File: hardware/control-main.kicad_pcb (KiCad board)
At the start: 2 copper layers, 71.1 x 72.4 mm, 32 parts, among them K1 CONN_3, P1 CONN_2, P2 CONN_6, P3 CONN_4, P4 CONN_4, P5 CONN_5, P6 CONN_5, SW1 SW_PUSH, SW2 SW_PUSH, SW3 SW_PUSH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

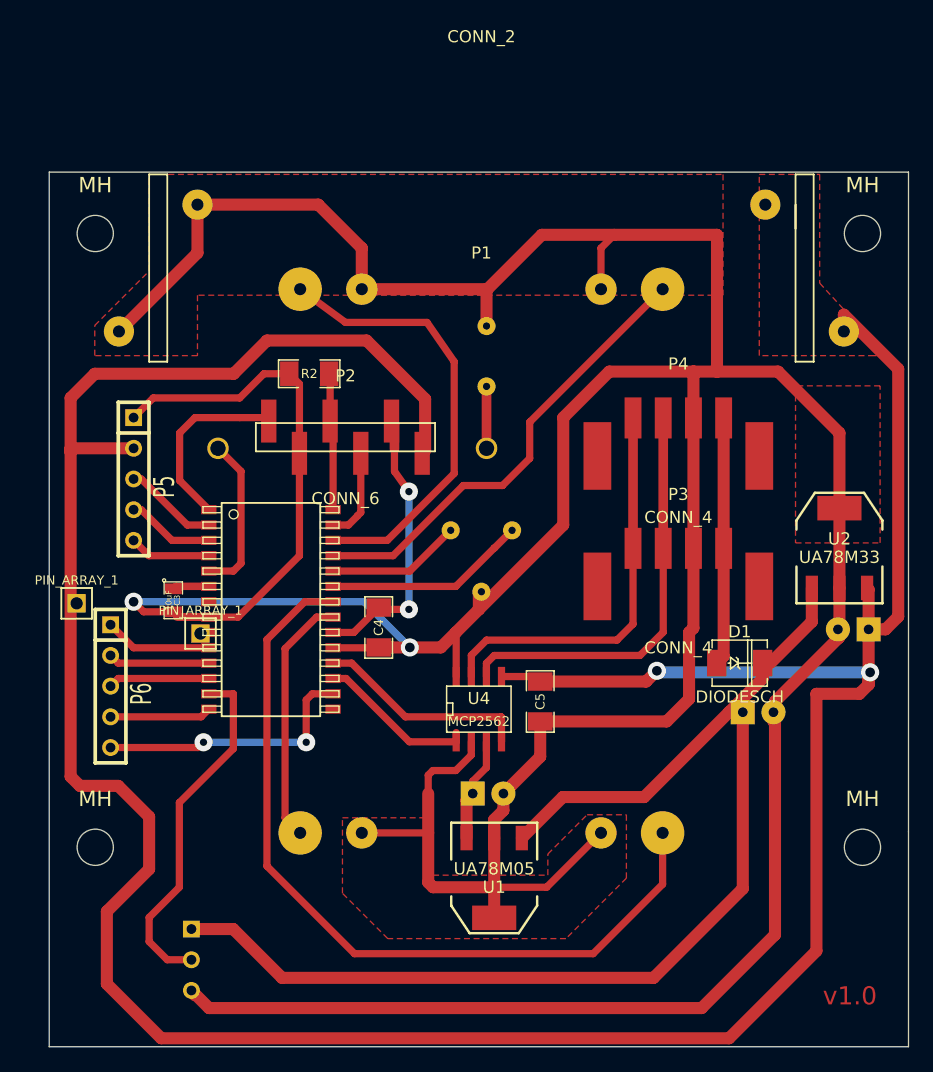
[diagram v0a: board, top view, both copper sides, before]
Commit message: Convert to kicad 6.x
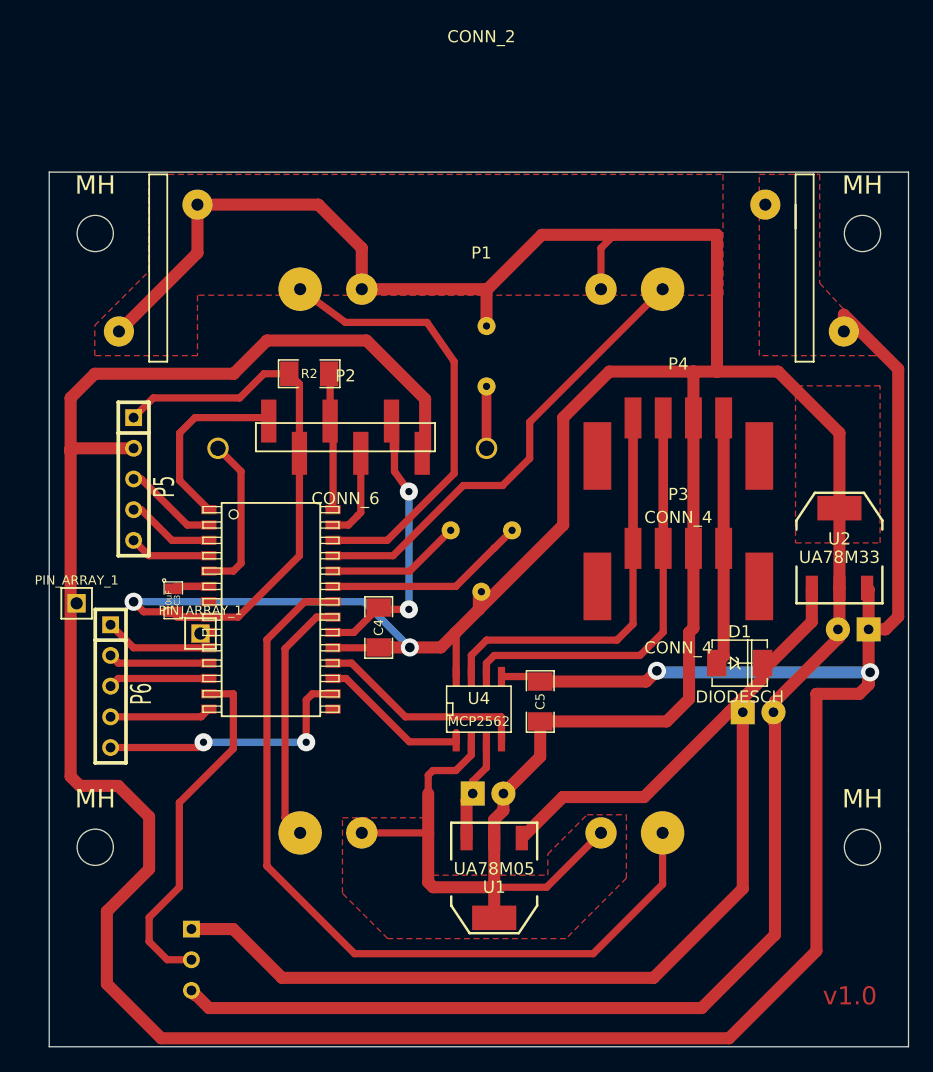
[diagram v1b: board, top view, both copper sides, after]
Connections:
- net /~MCLR renamed /~{MCLR}
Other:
- net class Default removed
